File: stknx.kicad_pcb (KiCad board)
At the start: 2 copper layers, 51.3 x 20.3 mm, 48 parts, among them J1 KNX, J2 PMOD, J3 VDDHV, J4 VCCCORE, J5 VDCDC, U1 STKNX

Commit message: A few DRC fixes
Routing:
- net GND: track 17.4 -> 16.3 mm

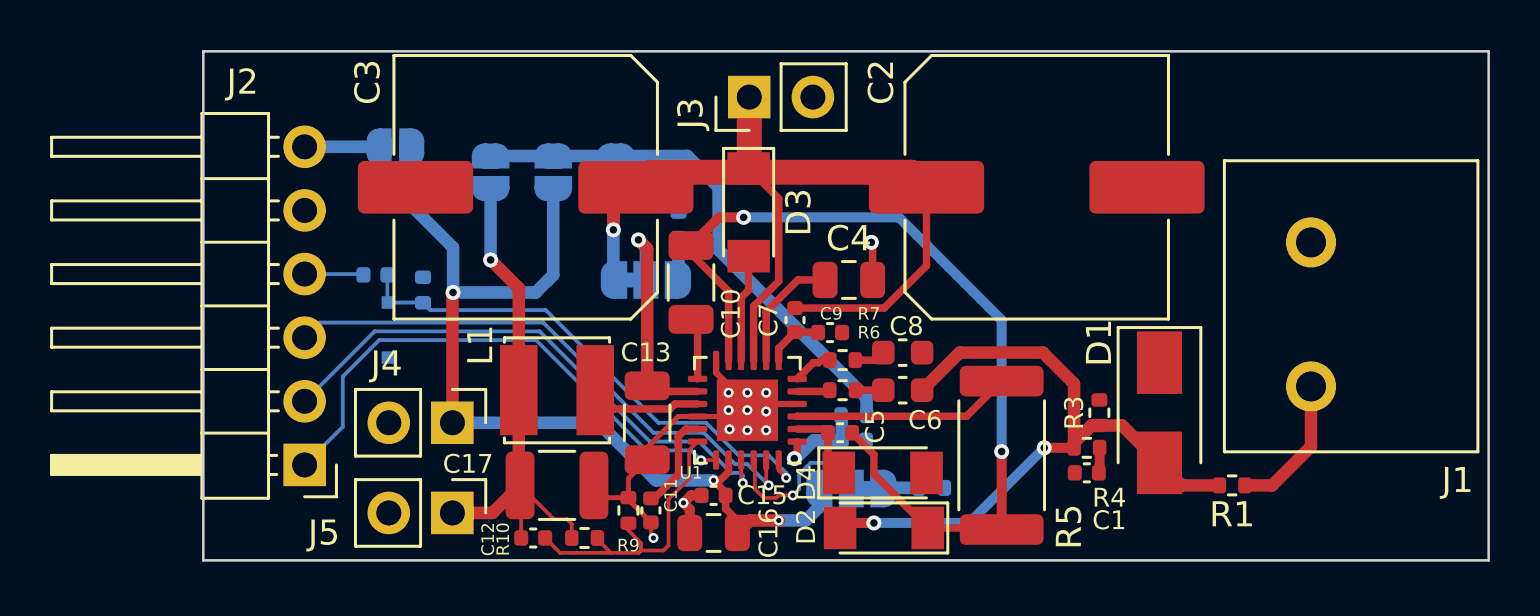
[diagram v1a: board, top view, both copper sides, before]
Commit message: improve GND connectivity a bit
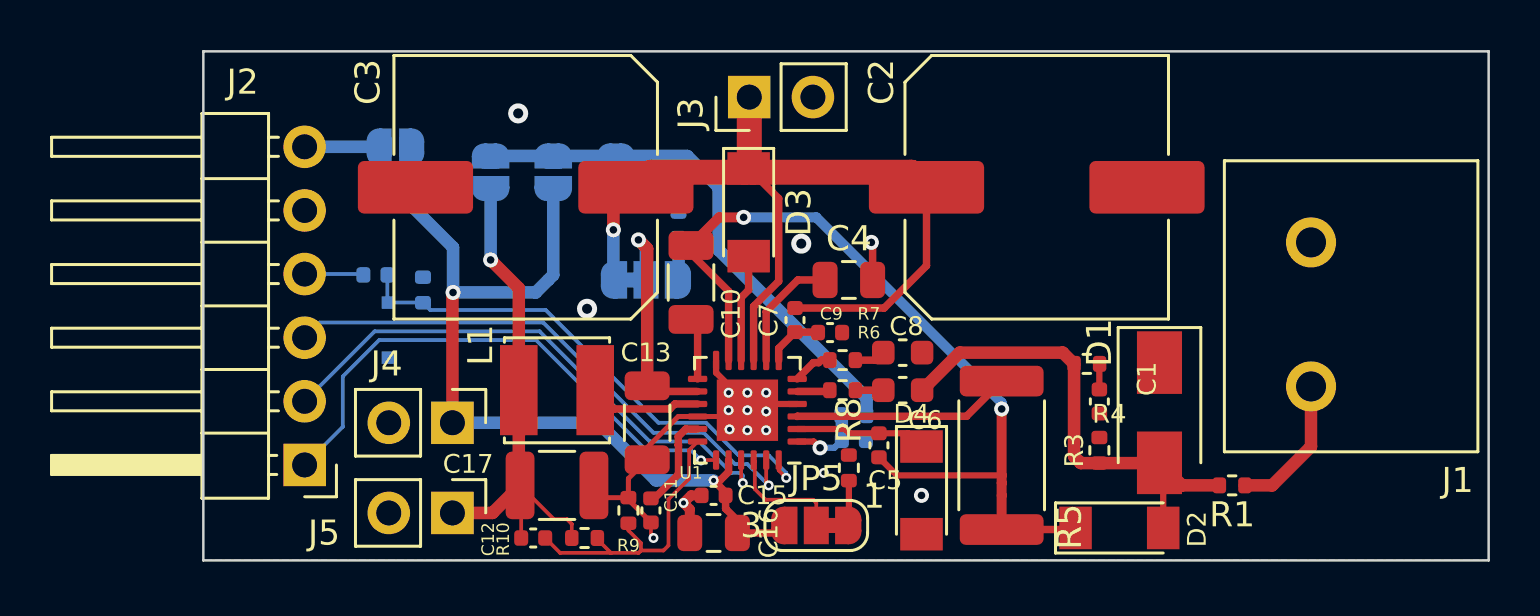
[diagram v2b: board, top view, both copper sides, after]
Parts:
- JP5, R8: moved to F.Cu
- moved D2 9.40 mm to (191.0, 115.8), turned to 0 degrees
- moved R8 3.40 mm to (180.2, 113.4), turned to -90 degrees
- moved R4 3.35 mm to (189.7, 109.2)
- moved C1 2.89 mm to (190.2, 110.8), turned to 90 degrees
- moved JP5 2.03 mm to (178.9, 115.7)
- moved D4 1.70 mm to (183.1, 114.3), turned to -90 degrees
- moved C5 1.63 mm to (181.4, 112.5), turned to 90 degrees
- moved R3 1.50 mm to (190.2, 112.7)
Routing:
- net Net-(C6-Pad1): track 27.7 -> 19.5 mm, vias 2 -> 0
- net /VCCCORE: track 38.7 -> 36.3 mm, vias 3 -> 2
- net /VCC_SEL: track 7.05 -> 4.76 mm, vias 1 -> 0
- net Net-(C5-Pad2): track 3.07 -> 5.25 mm
- net Net-(C10-Pad1): track 36.2 -> 34.5 mm
- net Net-(C14-Pad1): track 3.98 -> 3.02 mm
- net GND: vias 12 -> 17
